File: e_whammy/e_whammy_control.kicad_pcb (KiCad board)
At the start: 2 copper layers, 32 x 10 mm, 30 parts, among them J1 Conn_01x03, J2 Conn_01x03, U2 HT7550-1, U3 TLV9002IDGKR, U4 TPADG779BKSZ, U5 LM393BIDGKR, U6 REF3025

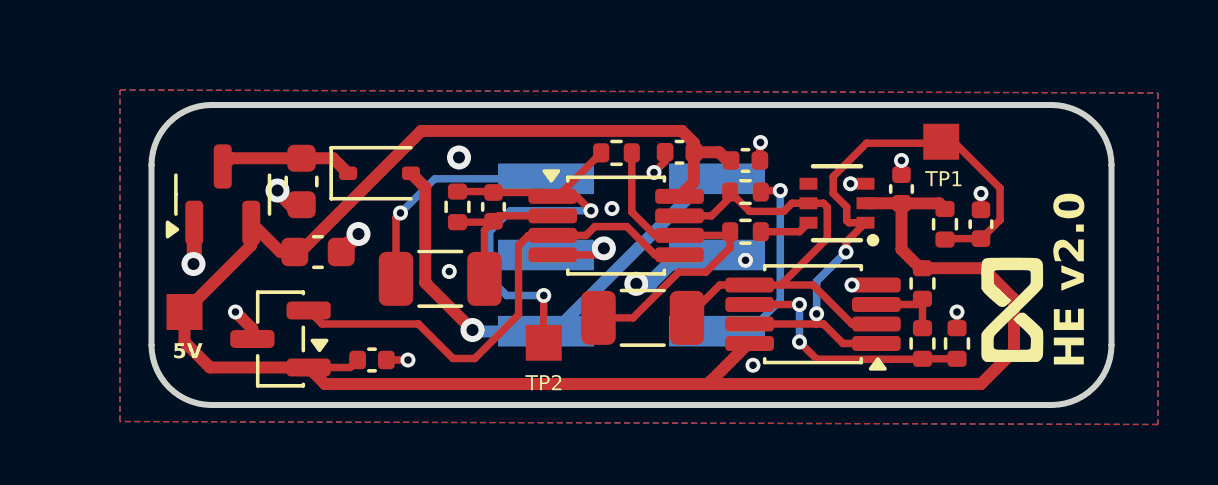
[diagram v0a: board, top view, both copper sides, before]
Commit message: Updated DC servo schematic for spice simulation
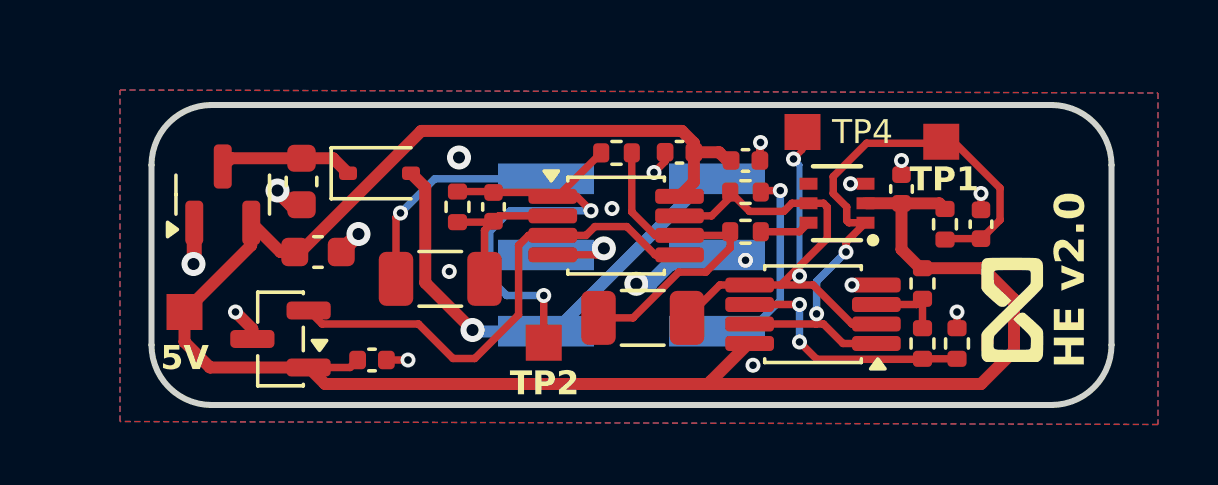
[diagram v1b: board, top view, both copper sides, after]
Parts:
- added TP4: TestPoint, cycfi_library:single-pad-1.2x1.2, F.Cu at (160.6, 141.9)
- R4: value 10M -> 1M
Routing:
- net INTEG_OUT: track 16.4 -> 21.4 mm, vias 0 -> 2
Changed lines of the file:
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@@
 			(effects
 				(font
-					(size 0.5 0.5)
-					(thickness 0.1)
+					(size 0.8 0.8)
+					(thickness 0.15)
+					(bold yes)
 				)
 			)
@@
 		(sheetname "/")
 		(sheetfile "e_whammy_control.kicad_sch")
-		(attr smd exclude_from_bom)
+		(attr smd exclude_from_pos_files exclude_from_bom)
 		(pad "1" smd rect
 			(at 0 0)
@@
 		(embedded_fonts no)
 	)
+	(footprint "cycfi_library:single-pad-1.2x1.2"
+		(layer "F.Cu")
+		(at 160.6 141.9)
+		(property "Reference" "TP4"
+			(at 2 0 0)
+			(layer "F.SilkS")
+			(effects
+				(font
+					(size 0.8 0.8)
+					(thickness 0.15)
+				)
+			)
+		)
+		(property "Value" "TestPoint"
+			(at 0 -2.54 0)
+			(layer "F.Fab")
+			(effects
+				(font
+					(size 1 1)
+					(thickness 0.15)
+				)
+			)
+		)
+		(property "Datasheet" "~"
+			(at 0 0 0)
+			(layer "F.Fab")
+			(hide yes)
+			(effects
+				(font
+					(size 1.27 1.27)
+					(thickness 0.15)
+				)
+			)
+		)
+		(property "Description" "test point"
+			(at 0 0 0)
+			(layer "F.Fab")
+			(hide yes)
+			(effects
+				(font
+					(size 1.27 1.27)
+					(thickness 0.15)
+				)
+			)
+		)
+		(property ki_fp_filters "Pin* Test*")
+		(sheetname "/")
+		(sheetfile "e_whammy_control.kicad_sch")
+		(attr smd exclude_from_bom)
+		(pad "1" smd rect
+			(at 0 0)
+			(size 1.2 1.2)
+			(layers "F.Cu" "F.Mask" "F.Paste")
+			(net 16 "INTEG_OUT")
+			(pinfunction "1")
+			(pintype "passive")
+		)
+		(embedded_fonts no)
+	)
 	(footprint "Resistor_SMD:R_0402_1005Metric"
 		(layer "F.Cu")
@@
 			)
 		)
-		(property "Value" "10M"
+		(property "Value" "1M"
 			(at 0 1.17 90)
 			(layer "F.Fab")
@@
 		(sheetname "/")
 		(sheetfile "e_whammy_control.kicad_sch")
-		(attr smd)
+		(attr smd exclude_from_pos_files exclude_from_bom)
 		(pad "1" smd rect
 			(at 0 0)
@@
 			(effects
 				(font
-					(size 0.5 0.5)
-					(thickness 0.1)
+					(size 0.8 0.8)
+					(thickness 0.15)
+					(bold yes)
 				)
 			)
@@
 		(sheetname "/")
 		(sheetfile "e_whammy_control.kicad_sch")
-		(attr smd exclude_from_bom)
+		(attr smd exclude_from_pos_files exclude_from_bom)
 		(pad "1" smd rect
 			(at 0 0 270)
@@
 			(layers "F.Cu" "F.Mask" "F.Paste")
 			(net 8 "Net-(C8-Pad2)")
-			(pintype "unspecified")
+			(pintype "input")
 		)
 		(pad "2" smd rect
@@
 			(layers "F.Cu" "F.Mask" "F.Paste")
 			(net 16 "INTEG_OUT")
-			(pintype "unspecified")
+			(pintype "bidirectional")
 		)
 		(pad "6" smd rect
@@
 			)
 		)
-		(property "Datasheet" "http://www.ti.com/lit/ds/symlink/ref3033.pdf"
+		(property "Datasheet" "https://www.ti.com/lit/ds/symlink/ref30.pdf"
 			(at 0 0 0)
 			(layer "F.Fab")
@@
 		(sheetname "/")
 		(sheetfile "e_whammy_control.kicad_sch")
-		(attr smd)
+		(attr smd exclude_from_pos_files exclude_from_bom)
 		(fp_line
 			(start 6.15 3.81)
@@
 		(sheetname "/")
 		(sheetfile "e_whammy_control.kicad_sch")
-		(attr smd)
+		(attr smd exclude_from_pos_files exclude_from_bom)
 		(fp_line
 			(start -2 2)
@@
 	)
 	(gr_text "5V"
-		(at 139.6 149.5 0)
+		(at 139.2 149.9 0)
 		(layer "F.SilkS")
 		(effects
 			(font
-				(size 0.5 0.5)
-				(thickness 0.1)
+				(size 0.8 0.8)
+				(thickness 0.15)
 				(bold yes)
 			)
@@
 	)
 	(segment
+		(start 160.6 142.5)
+		(end 160.3 142.8)
+		(width 0.2)
+		(layer "F.Cu")
+		(net 16)
+	)
+	(segment
 		(start 161.302001 144.275)
 		(end 160.8 144.275)
@@
 	)
 	(segment
+		(start 160.6 141.9)
+		(end 160.6 142.5)
+		(width 0.2)
+		(layer "F.Cu")
+		(net 16)
+	)
+	(segment
 		(start 160.95 147)
 		(end 159.876999 147)
@@
 		(net 16)
 	)
+	(via
+		(at 160.3 142.8)
+		(size 0.5)
+		(drill 0.25)
+		(layers "F.Cu" "B.Cu")
+		(net 16)
+	)
+	(via
+		(at 160.5 146.7)
+		(size 0.5)
+		(drill 0.25)
+		(layers "F.Cu" "B.Cu")
+		(net 16)
+	)
+	(segment
+		(start 160.3 142.8)
+		(end 160.5 143)
+		(width 0.2)
+		(layer "B.Cu")
+		(net 16)
+	)
+	(segment
+		(start 160.5 143)
+		(end 160.5 146.7)
+		(width 0.2)
+		(layer "B.Cu")
+		(net 16)
+	)

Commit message: Updates using DC servo mechanism
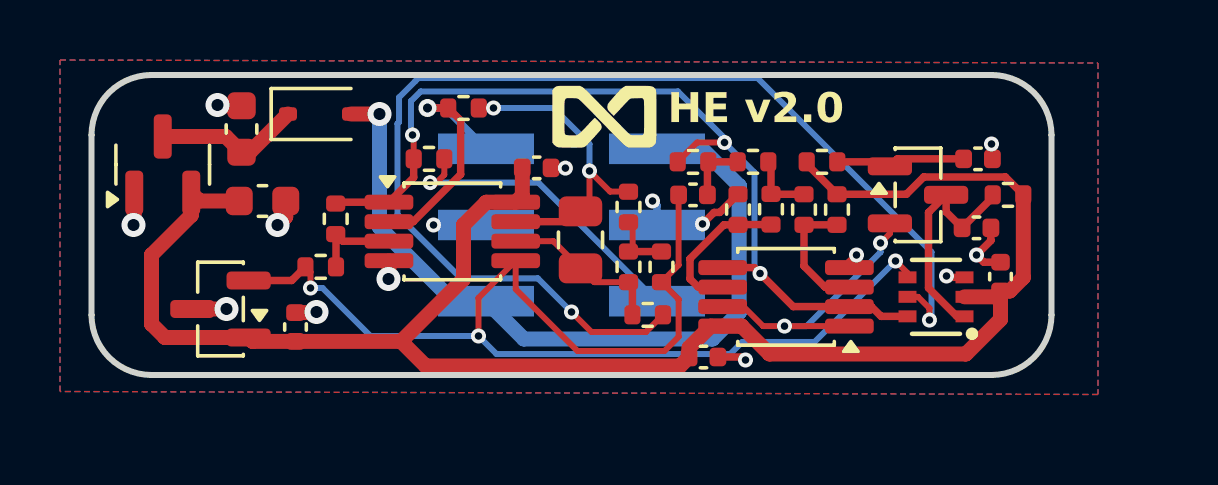
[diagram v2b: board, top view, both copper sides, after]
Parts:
- removed C6, C9: 100nF (COG), Capacitor_SMD:C_1206_3216Metric
- removed C7: 1nF (COG), Capacitor_SMD:C_0402_1005Metric
- removed R4: 1M, Resistor_SMD:R_0402_1005Metric
- removed R6: 100k, Resistor_SMD:R_0402_1005Metric
- removed R7: 2M, Resistor_SMD:R_0402_1005Metric
- removed R8: 1K, Resistor_SMD:R_0402_1005Metric
- removed TP1, TP2, TP3, TP4: TestPoint, cycfi_library:single-pad-1.2x1.2
- added C11: 2.2uF, Capacitor_SMD:C_0402_1005Metric, F.Cu at (156.9, 144.0)
- added C12: 10uF, Capacitor_SMD:C_0805_2012Metric, F.Cu at (153.2, 145.5)
- added C13: 2.2uF, Capacitor_SMD:C_0402_1005Metric, F.Cu at (166.4, 142.8)
- added Q1: 2N7002, Package_TO_SOT_SMD:SOT-23, F.Cu at (164.4, 144.0)
- added R10: 200k, Resistor_SMD:R_0402_1005Metric, F.Cu at (158.9, 142.9)
- added R11: 100k, Resistor_SMD:R_0402_1005Metric, F.Cu at (156.9, 142.9)
- added R12: 47k, Resistor_SMD:R_0402_1005Metric, F.Cu at (149.3, 141.1)
- added R13: 1k, Resistor_SMD:R_0402_1005Metric, F.Cu at (144.5, 146.4)
- added R14: 100k, Resistor_SMD:R_0402_1005Metric, F.Cu at (155.4, 148.0)
- added R15: 20k, Resistor_SMD:R_0402_1005Metric, F.Cu at (145.0, 144.8)
- added R16: 100k, Resistor_SMD:R_0402_1005Metric, F.Cu at (154.8, 146.4)
- added R17: 100k, Resistor_SMD:R_0402_1005Metric, F.Cu at (154.8, 144.4)
- added R18: 470Ω, Resistor_SMD:R_0402_1005Metric, F.Cu at (155.9, 146.4)
- added R19: 1K, Resistor_SMD:R_0402_1005Metric, F.Cu at (148.2, 142.8)
- added R20: 1M, Resistor_SMD:R_0402_1005Metric, F.Cu at (161.2, 142.9)
- added R9: 4.7k, Resistor_SMD:R_0402_1005Metric, F.Cu at (159.6, 144.5)
- R2: value 10k -> 4.7k
- moved G*** 15.0 mm to (154.0, 141.4), turned to 0 degrees
- moved R3 8.56 mm to (158.4, 144.5)
- moved C3 6.96 mm to (151.7, 143.1)
- moved C4 6.87 mm to (157.3, 149.4), turned to 180 degrees
- moved R2 5.96 mm to (160.7, 144.5), turned to -90 degrees
- moved U3 5.46 mm to (148.9, 145.2)
- moved U4 4.54 mm to (165.1, 147.4)
- moved C5 4.41 mm to (167.2, 146.7)
- moved R1 3.77 mm to (161.8, 144.5)
- moved D1 2.81 mm to (144.5, 141.3)
- moved C10 2.78 mm to (143.7, 148.4), turned to -90 degrees
- moved C1 2.66 mm to (141.9, 141.8), turned to 90 degrees
- moved C2 2.51 mm to (142.6, 144.2)
- moved R5 2.32 mm to (167.4, 144.0), turned to 0 degrees
- moved J1 2.24 mm to (150.1, 145.0)
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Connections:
- net 5v renamed +5V
- net Net-(U5A-+) renamed /WHI
- C8 pad 2: Net-(C8-Pad2) -> RESET
- J2 pad 1: OUT -> Net-(J2-Pin_1)
- R2 pad 1: Net-(U5B--) -> Net-(R10-Pad1)
- R3 pad 2: Net-(U5B--) -> /WLO
- R5 pad 1: Net-(C8-Pad2) -> RESET
- U3 pad 1: Net-(C7-Pad2) -> OUT
- U3 pad 2: Net-(U3A--) -> HE_SENSOR
- U3 pad 3: VREF -> Net-(U3A-+)
- U3 pad 7: INTEG_OUT -> Net-(C12-Pad1)
- U4 pad 1: Net-(C8-Pad2) -> RESET
- U4 pad 4: unconnected-(U4-Pad4) -> VREF
- U4 pad 5: INTEG_OUT -> INTEG_IN
- U4 pad 6: RESET -> OUT
- U5 pad 1: Net-(C8-Pad2) -> WINDOW
- U5 pad 2: INTEG_OUT -> OUT
- U5 pad 5: INTEG_OUT -> OUT
- U5 pad 6: Net-(U5B--) -> /WLO
- U5 pad 7: Net-(C8-Pad2) -> WINDOW
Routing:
- net INTEG_IN: track 0.00 -> 38.6 mm, vias 0 -> 2
- net VREF: track 16.6 -> 40.9 mm, vias 0 -> 3
- net OUT: track 6.87 -> 30.2 mm, vias 1 -> 3
- net INTEG_OUT: track 21.4 -> 0.00 mm, vias 2 -> 0
- net Net-(C8-Pad2): track 20.7 -> 0.00 mm, vias 2 -> 0
- net Net-(C7-Pad2): track 15.8 -> 0.00 mm, vias 2 -> 0
- net Net-(C12-Pad1): track 0.00 -> 10.6 mm, vias 0 -> 2
- net Net-(J2-Pin_1): track 0.00 -> 10.4 mm, vias 0 -> 1
- net WINDOW: track 0.00 -> 9.81 mm, vias 0 -> 2
- net V+: track 16.4 -> 26.1 mm
- net +5V: track 68.0 -> 59.3 mm
- net Net-(U5B--): track 8.45 -> 0.00 mm, vias 2 -> 0
- net RESET: track 1.71 -> 7.78 mm
- net Net-(U3B--): track 11.5 -> 5.54 mm
- net Net-(U3A--): track 5.31 -> 0.00 mm
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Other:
- board text removed: "5V"
